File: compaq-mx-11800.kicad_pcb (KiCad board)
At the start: 2 copper layers, 389.5 x 166.4 mm, 238 parts

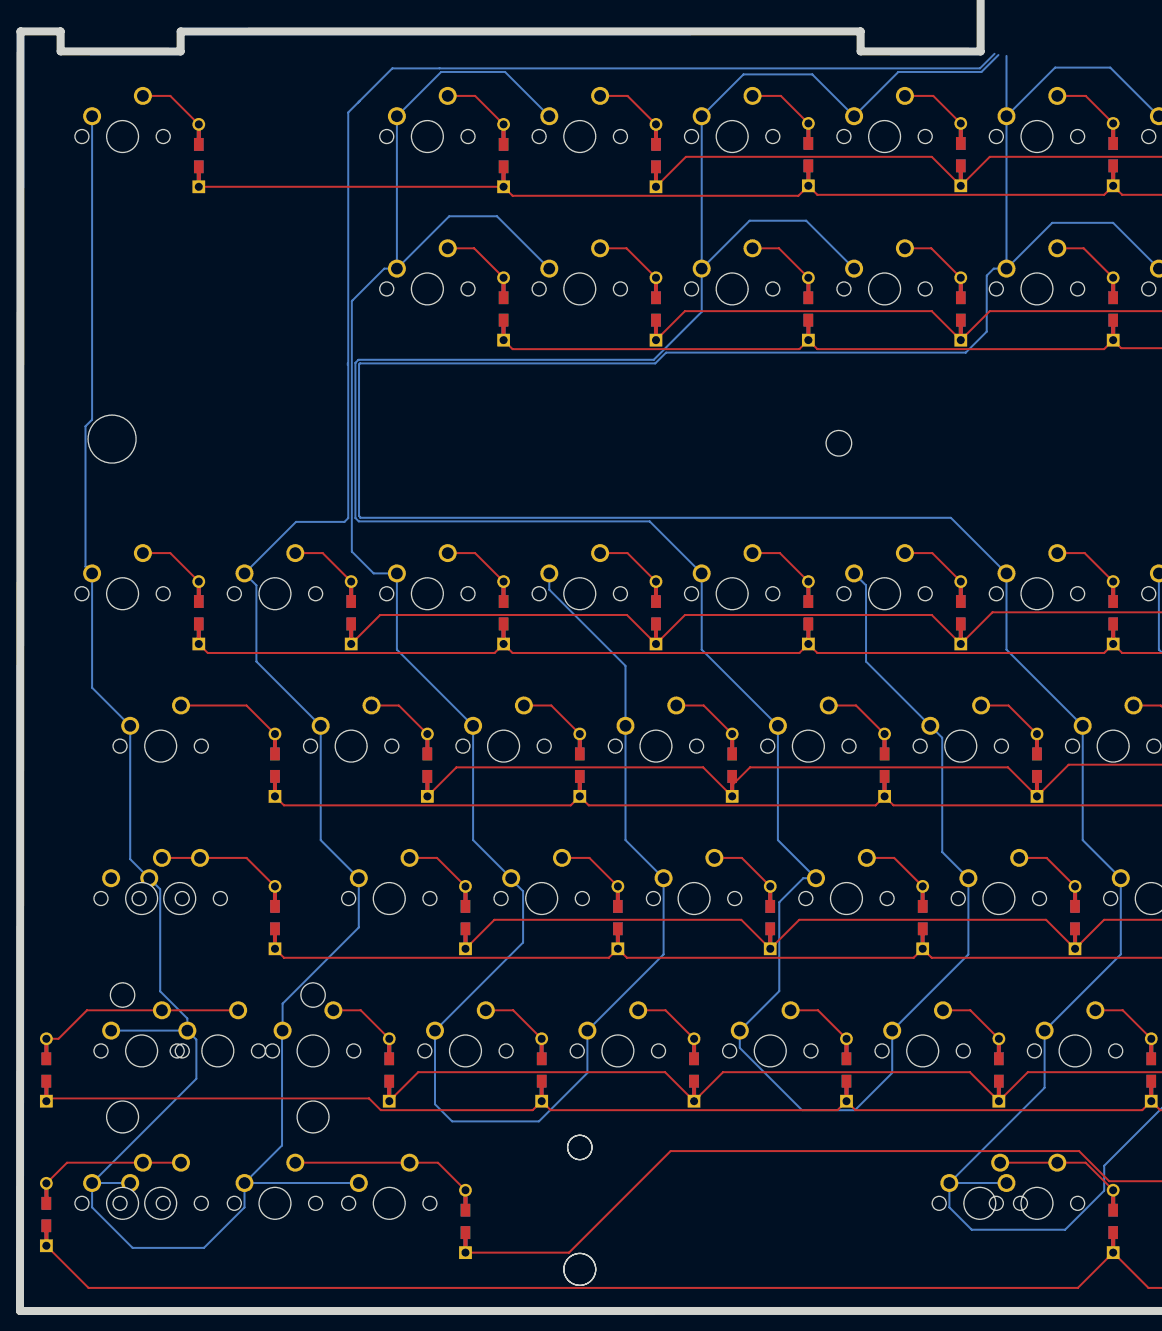
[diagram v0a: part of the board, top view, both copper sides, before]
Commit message: route row traces to top
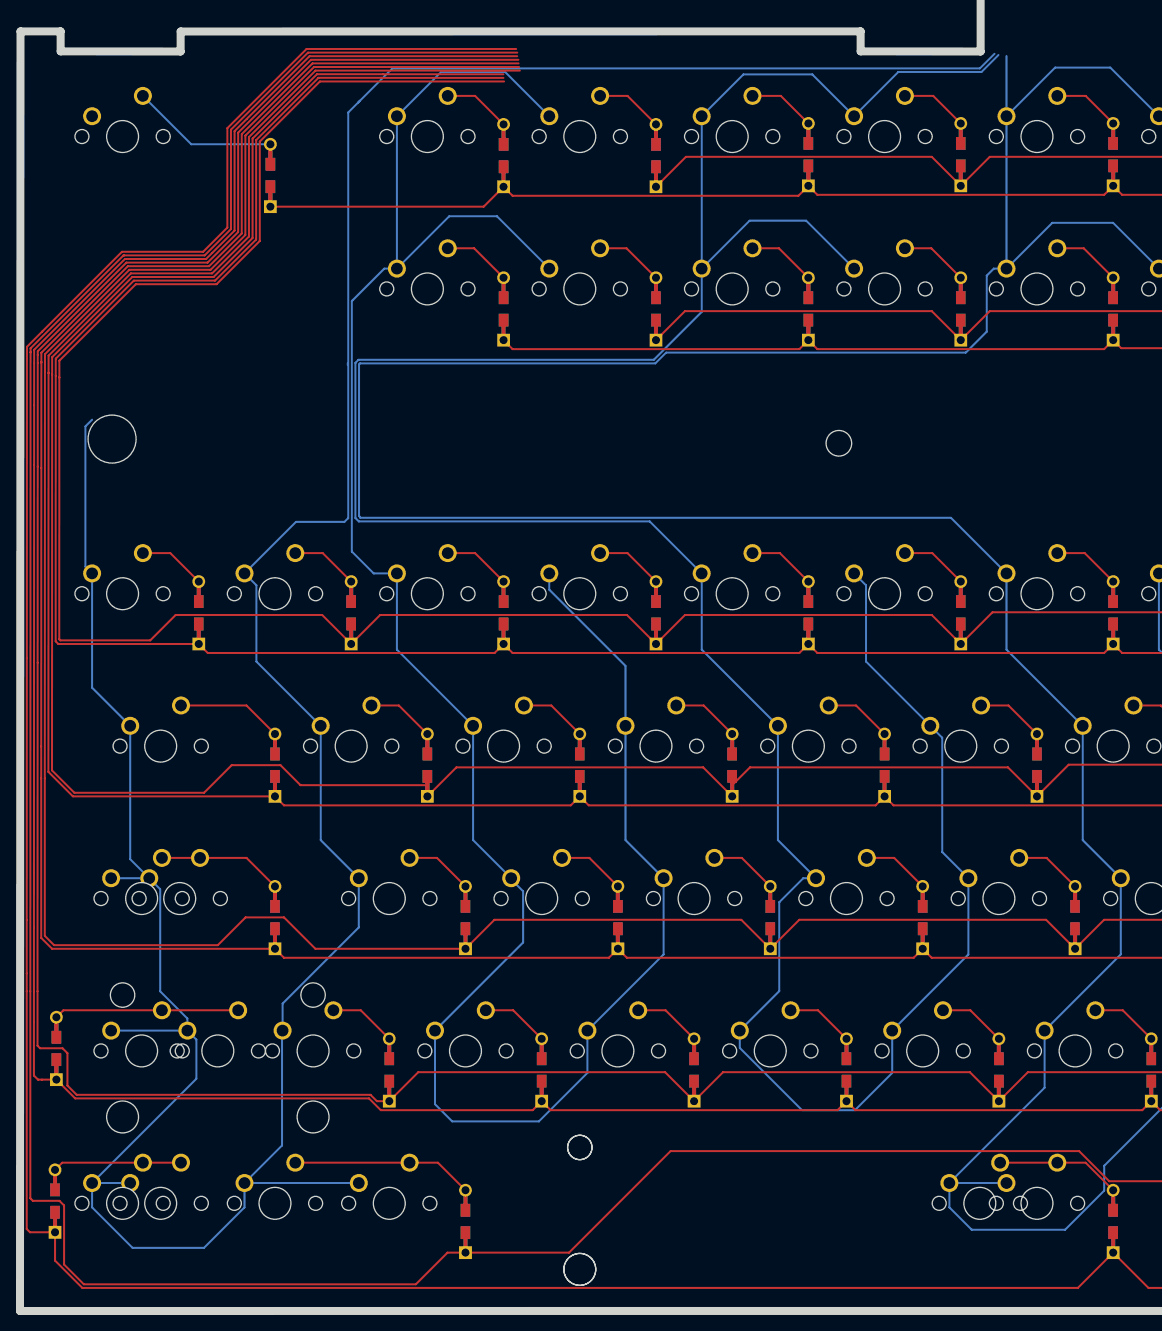
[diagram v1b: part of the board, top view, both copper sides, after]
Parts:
- moved D1 9.29 mm to (-14.9, 64.4)
- moved D94 2.97 mm to (-41.6, 173.5)
- moved D121 2.00 mm to (-41.8, 192.6)
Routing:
- net Net-(D115-Pad1): track 365.5 -> 620.0 mm
- net Net-(D101-Pad1): track 408.1 -> 626.6 mm
- net Net-(D55-Pad1): track 372.7 -> 582.9 mm
- net Net-(D108-Pad1): track 458.3 -> 657.8 mm
- net Net-(D54-Pad1): track 353.1 -> 538.0 mm
- net Net-(D36-Pad1): track 384.6 -> 565.1 mm
- net Net-(D100-Pad1): track 473.6 -> 649.8 mm
- net Net-(D33-Pad1): track 428.7 -> 591.3 mm
- net Net-(D31-Pad1): track 337.8 -> 489.3 mm
- net Net-(D34-Pad1): track 335.4 -> 466.5 mm
- net Net-(MX1-Pad1): track 441.7 -> 408.5 mm
- net Net-(D1-Pad2): track 8.46 -> 18.4 mm
- net Net-(D1-Pad1): track 351.6 -> 343.7 mm
- net Net-(D94-Pad2): track 25.4 -> 23.1 mm
- net Net-(D121-Pad2): track 17.9 -> 16.1 mm
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
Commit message: modify column traces
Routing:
- net Net-(MX1-Pad1): track 408.5 -> 837.3 mm
- net Net-(MX18-Pad1): track 286.3 -> 617.2 mm
- net Net-(MX114-Pad1): track 466.6 -> 742.2 mm
- net Net-(MX20-Pad1): track 371.2 -> 555.5 mm
- net Net-(MX106-Pad1): track 514.0 -> 366.0 mm
- net Net-(MX102-Pad1): track 238.1 -> 347.0 mm
- net Net-(MX108-Pad1): track 470.8 -> 546.3 mm
- net Net-(MX17-Pad1): track 463.5 -> 517.9 mm
- net Net-(MX100-Pad1): track 483.0 -> 515.9 mm
- net Net-(MX10-Pad1): track 406.8 -> 428.5 mm

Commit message: traces cleanup
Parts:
- moved D124 64.9 mm to (264.3, 214.9)
- moved D46 64.9 mm to (209.5, 138.6)
- moved D51 64.9 mm to (304.8, 138.6)
- moved D54 64.9 mm to (345.3, 138.6)
- moved D55 64.9 mm to (364.3, 138.6)
- moved D57 64.9 mm to (382.2, 154.7)
- moved D74 64.9 mm to (304.8, 176.7)
- moved D91 64.9 mm to (364.3, 155.3)
- moved MX108 64.9 mm to (305.1, 199.2)
- moved MX124 64.9 mm to (257.2, 212.4)
- moved MX33 64.9 mm to (392.9, 117.2)
- moved MX57 64.9 mm to (392.9, 155.3)
- moved MX67 64.9 mm to (209.5, 155.3)
- moved MX74 64.9 mm to (292.9, 164.8)
- moved MX86 64.9 mm to (233.4, 174.3)
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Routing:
- net Net-(MX114-Pad1): track 742.2 -> 520.0 mm
- net Net-(D31-Pad1): track 489.3 -> 665.4 mm
- net Net-(D34-Pad1): track 466.5 -> 610.0 mm
- net Net-(D36-Pad1): track 565.1 -> 671.9 mm
- net Net-(D100-Pad1): track 649.8 -> 756.5 mm
- net Net-(D108-Pad1): track 657.8 -> 758.0 mm
- net Net-(D18-Pad1): track 318.1 -> 404.2 mm
- net Net-(D115-Pad1): track 620.0 -> 706.1 mm
- net Net-(D55-Pad1): track 582.9 -> 648.0 mm
- net Net-(D33-Pad1): track 591.3 -> 653.4 mm
- net Net-(D54-Pad1): track 538.0 -> 598.5 mm
- net Net-(D101-Pad1): track 626.6 -> 687.0 mm
- net Net-(MX108-Pad1): track 546.3 -> 487.7 mm
- net Net-(D19-Pad1): track 329.8 -> 384.9 mm
- net Net-(D1-Pad1): track 343.7 -> 383.2 mm
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
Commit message: trace correction
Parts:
- moved D31 26.5 mm to (307.6, 138.6), turned to 270 degrees
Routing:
- net Net-(MX108-Pad1): track 487.7 -> 462.1 mm
- net Net-(D31-Pad2): track 18.0 -> 35.6 mm
- net Net-(D55-Pad1): track 648.0 -> 643.8 mm
- net Net-(D31-Pad1): track 665.4 -> 663.7 mm
- net Net-(D54-Pad1): track 598.5 -> 596.9 mm
- net Net-(D36-Pad1): track 671.9 -> 670.7 mm
- net Net-(MX17-Pad1): track 517.9 -> 518.6 mm

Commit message: connect rows to output pins
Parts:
- added J1: Conn_01x16_Female, Connector_PinHeader_2.54mm:PinHeader_1x16_P2.54mm_Vertical, F.Cu at (171.2, 63.9)
- added J2: Conn_01x16_Female, Connector_PinHeader_2.54mm:PinHeader_1x16_P2.54mm_Vertical, F.Cu at (215.1, 63.9)
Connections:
- net Net-(D1-Pad1) renamed row14
- net Net-(D100-Pad1) renamed row3
- net Net-(D101-Pad1) renamed row2
- net Net-(D108-Pad1) renamed row0
- net Net-(D11-Pad1) renamed row13
- net Net-(D115-Pad1) renamed row1
- net Net-(D18-Pad1) renamed row12
- net Net-(D19-Pad1) renamed row11
- net Net-(D31-Pad1) renamed row10
- net Net-(D33-Pad1) renamed row7
- net Net-(D34-Pad1) renamed row9
- net Net-(D36-Pad1) renamed row8
- net Net-(D54-Pad1) renamed row5
- net Net-(D55-Pad1) renamed row6
- net Net-(MX1-Pad1) renamed col0
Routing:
- net row0: track 758.0 -> 835.8 mm
- net row1: track 706.1 -> 780.5 mm
- net row2: track 687.0 -> 755.5 mm
- net row5: track 596.9 -> 663.0 mm
- net row6: track 643.8 -> 706.8 mm
- net row10: track 663.7 -> 711.2 mm
- net row9: track 610.0 -> 653.6 mm
- net row8: track 670.7 -> 712.5 mm
- net row7: track 653.4 -> 692.2 mm
- net row3: track 756.5 -> 786.4 mm
- net row12: track 404.2 -> 429.6 mm
- net row11: track 384.9 -> 406.5 mm
- net row14: track 383.2 -> 399.3 mm
- net row13: track 344.5 -> 356.2 mm

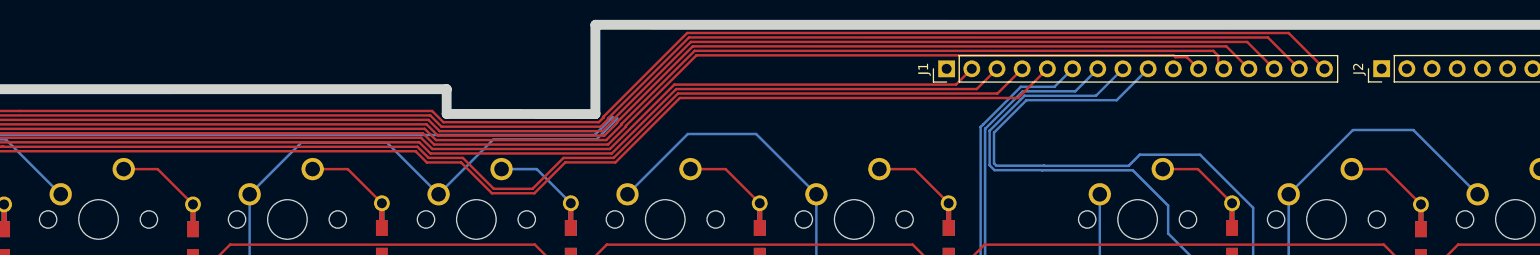
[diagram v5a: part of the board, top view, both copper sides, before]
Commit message: fix some traces and stabilizer holes
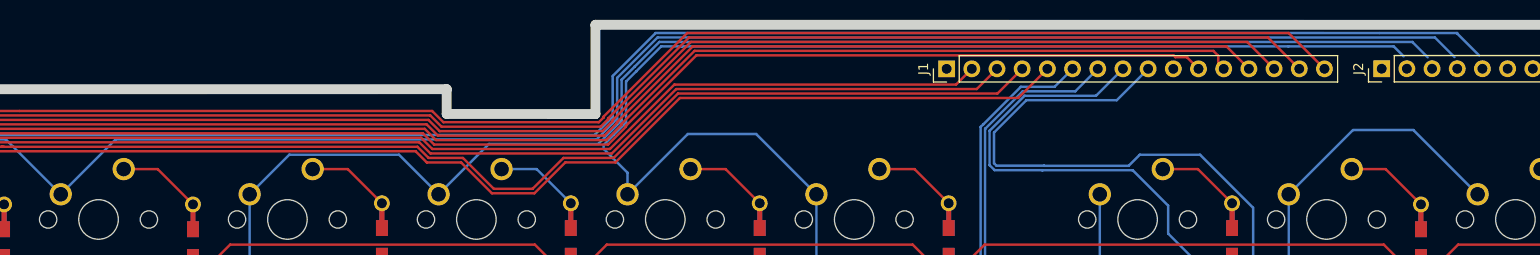
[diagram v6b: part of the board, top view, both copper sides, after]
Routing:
- net Net-(MX18-Pad1): track 617.2 -> 767.5 mm
- net col0: track 816.5 -> 910.8 mm
- net Net-(MX100-Pad1): track 508.1 -> 601.7 mm
- net Net-(MX20-Pad1): track 555.5 -> 642.5 mm
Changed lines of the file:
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@@
     (thickness 1.6)
     (drawings 27)
-    (tracks 1656)
+    (tracks 1689)
     (zones 0)
     (modules 240)
@@
   (page A3)
   (layers
-    (0 F.Cu signal)
+    (0 F.Cu signal hide)
     (31 B.Cu signal)
     (32 B.Adhes user)
@@
   (segment (start 90.78379 124.78996) (end 250.99004 124.78996) (width 0.25) (layer B.Cu) (net 100))
   (segment (start 81.9125 133.66125) (end 90.78379 124.78996) (width 0.25) (layer B.Cu) (net 100))
-  (segment (start 120.0125 76.51125) (end 114.79 71.28875) (width 0.25) (layer B.Cu) (net 101))
-  (segment (start 106.185 71.28875) (end 100.9625 76.51125) (width 0.25) (layer B.Cu) (net 101))
-  (segment (start 114.79 71.28875) (end 106.185 71.28875) (width 0.25) (layer B.Cu) (net 101))
+  (segment (start 81.9125 76.51125) (end 87.44375 70.98) (width 0.25) (layer B.Cu) (net 100))
+  (segment (start 87.44375 70.98) (end 135.936411 70.979999) (width 0.25) (layer B.Cu) (net 100))
+  (segment (start 135.936411 70.979999) (end 137.570705 69.345705) (width 0.25) (layer B.Cu) (net 100))
+  (segment (start 137.570705 69.345705) (end 138.02001 68.8964) (width 0.25) (layer B.Cu) (net 100))
+  (segment (start 138.02001 68.8964) (end 138.02001 64.7664) (width 0.25) (layer B.Cu) (net 100))
+  (segment (start 138.02001 64.7664) (end 142.090965 60.695446) (width 0.25) (layer B.Cu) (net 100))
+  (segment (start 220.475777 60.700777) (end 222.449999 62.674999) (width 0.25) (layer B.Cu) (net 100))
+  (segment (start 142.090965 60.695446) (end 220.475777 60.700777) (width 0.25) (layer B.Cu) (net 100))
   (segment (start 100.9625 76.51125) (end 100.9625 95.56125) (width 0.25) (layer B.Cu) (net 101))
   (segment (start 120.0125 95.56125) (end 114.02125 89.57) (width 0.25) (layer B.Cu) (net 101))
@@
   (segment (start 121.503599 144.677349) (end 121.503599 135.152349) (width 0.25) (layer B.Cu) (net 101))
   (segment (start 129.5375 152.71125) (end 121.503599 144.677349) (width 0.25) (layer B.Cu) (net 101))
-  (segment (start 120.0125 76.51125) (end 125.54375 70.98) (width 0.25) (layer B.Cu) (net 101))
-  (segment (start 135.936411 70.979999) (end 138.06 68.85641) (width 0.25) (layer B.Cu) (net 101))
-  (segment (start 125.54375 70.98) (end 135.936411 70.979999) (width 0.25) (layer B.Cu) (net 101))
   (segment (start 120.0125 98.6225) (end 120.0125 95.56125) (width 0.25) (layer B.Cu) (net 101))
   (segment (start 128.72002 107.33002) (end 120.0125 98.6225) (width 0.25) (layer B.Cu) (net 101))
@@
   (segment (start 128.43378 125.23997) (end 251.49003 125.23997) (width 0.25) (layer B.Cu) (net 101))
   (segment (start 120.0125 133.66125) (end 128.43378 125.23997) (width 0.25) (layer B.Cu) (net 101))
+  (segment (start 116.022499 72.521249) (end 120.0125 76.51125) (width 0.25) (layer B.Cu) (net 101))
+  (segment (start 104.952501 72.521249) (end 116.022499 72.521249) (width 0.25) (layer B.Cu) (net 101))
+  (segment (start 100.9625 76.51125) (end 104.952501 72.521249) (width 0.25) (layer B.Cu) (net 101))
+  (segment (start 142.279532 61.145469) (end 218.200631 61.150631) (width 0.25) (layer B.Cu) (net 101))
+  (segment (start 139.77282 63.65) (end 139.775 63.65) (width 0.25) (layer B.Cu) (net 101))
+  (segment (start 218.200631 61.150631) (end 219.75 62.7) (width 0.25) (layer B.Cu) (net 101))
+  (segment (start 138.470019 64.952801) (end 139.77282 63.65) (width 0.25) (layer B.Cu) (net 101))
+  (segment (start 138.470019 69.082801) (end 138.470019 64.952801) (width 0.25) (layer B.Cu) (net 101))
+  (segment (start 136.122812 71.430008) (end 138.470019 69.082801) (width 0.25) (layer B.Cu) (net 101))
+  (segment (start 139.775 63.65) (end 142.279532 61.145469) (width 0.25) (layer B.Cu) (net 101))
+  (segment (start 125.093742 71.430008) (end 136.122812 71.430008) (width 0.25) (layer B.Cu) (net 101))
+  (segment (start 120.0125 76.51125) (end 125.093742 71.430008) (width 0.25) (layer B.Cu) (net 101))
   (segment (start 274 188.27125) (end 264.475 188.27125) (width 0.25) (layer F.Cu) (net 102))
   (segment (start 264.475 188.27125) (end 263.18595 188.27125) (width 0.25) (layer F.Cu) (net 102))
@@
   (segment (start 141.038751 91.571249) (end 154.122499 91.571249) (width 0.25) (layer B.Cu) (net 104))
   (segment (start 139.0625 93.5475) (end 141.038751 91.571249) (width 0.25) (layer B.Cu) (net 104))
+  (segment (start 139.0625 76.51125) (end 139.0625 74.3375) (width 0.25) (layer B.Cu) (net 104))
+  (segment (start 136.65 71.925) (end 136.65 71.53923) (width 0.25) (layer B.Cu) (net 104))
+  (segment (start 139.0625 74.3375) (end 136.65 71.925) (width 0.25) (layer B.Cu) (net 104))
+  (segment (start 136.65 71.53923) (end 137.66423 70.525) (width 0.25) (layer B.Cu) (net 104))
+  (segment (start 137.66423 70.525) (end 138.920029 69.269201) (width 0.25) (layer B.Cu) (net 104))
+  (segment (start 138.920029 69.269201) (end 138.920029 65.139201) (width 0.25) (layer B.Cu) (net 104))
+  (segment (start 139.961401 64.100009) (end 142.465919 61.595492) (width 0.25) (layer B.Cu) (net 104))
+  (segment (start 139.95922 64.10001) (end 139.961401 64.100009) (width 0.25) (layer B.Cu) (net 104))
+  (segment (start 138.920029 65.139201) (end 139.95922 64.10001) (width 0.25) (layer B.Cu) (net 104))
+  (segment (start 142.465919 61.595492) (end 144.549972 61.595634) (width 0.25) (layer B.Cu) (net 104))
+  (segment (start 144.549972 61.595634) (end 205.699982 61.59979) (width 0.25) (layer B.Cu) (net 104))
+  (segment (start 205.699982 61.59979) (end 216.325512 61.600512) (width 0.25) (layer B.Cu) (net 104))
+  (segment (start 216.325512 61.600512) (end 217.325 62.6) (width 0.25) (layer B.Cu) (net 104))
   (segment (start 186.6875 76.51125) (end 186.6875 95.56125) (width 0.25) (layer B.Cu) (net 105))
   (segment (start 177.1625 143.18625) (end 186.6875 152.71125) (width 0.25) (layer B.Cu) (net 105))
@@
   (segment (start 39.388 95.25995) (end 43.469954 91.177996) (width 0.25) (layer F.Cu) (net 143))
   (segment (start 171.1 64) (end 171.24 63.86) (width 0.25) (layer F.Cu) (net 120))
+  (segment (start 137.57 64.58) (end 141.904578 60.245423) (width 0.25) (layer B.Cu) (net 137))
+  (segment (start 137.57 68.71) (end 137.57 64.58) (width 0.25) (layer B.Cu) (net 137))
+  (segment (start 141.904578 60.245423) (end 214.900388 60.250388) (width 0.25) (layer B.Cu) (net 137))
+  (segment (start 214.900388 60.250388) (end 222.725921 60.250921) (width 0.25) (layer B.Cu) (net 137))
+  (segment (start 222.725921 60.250921) (end 222.725921 60.300921) (width 0.25) (layer B.Cu) (net 137))
+  (segment (start 222.725921 60.300921) (end 224.95 62.525) (width 0.25) (layer B.Cu) (net 137))
   (segment (start 172.19 65.45) (end 173.78 63.86) (width 0.25) (layer F.Cu) (net 144))
   (segment (start 143.78552 65.45) (end 172.19 65.45) (width 0.25) (layer F.Cu) (net 144))
